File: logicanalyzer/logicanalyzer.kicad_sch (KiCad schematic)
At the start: 104 parts, among them J1 Conn_02x17_Odd_Even, J2 Conn_01x30_Pin, U1 74HC04, U2 74HC595, U3 74HC595, U4 74HC86, U5 74HC251, U6 74HC32, U7 74HC86, U8 74HC251, U9 74HC251

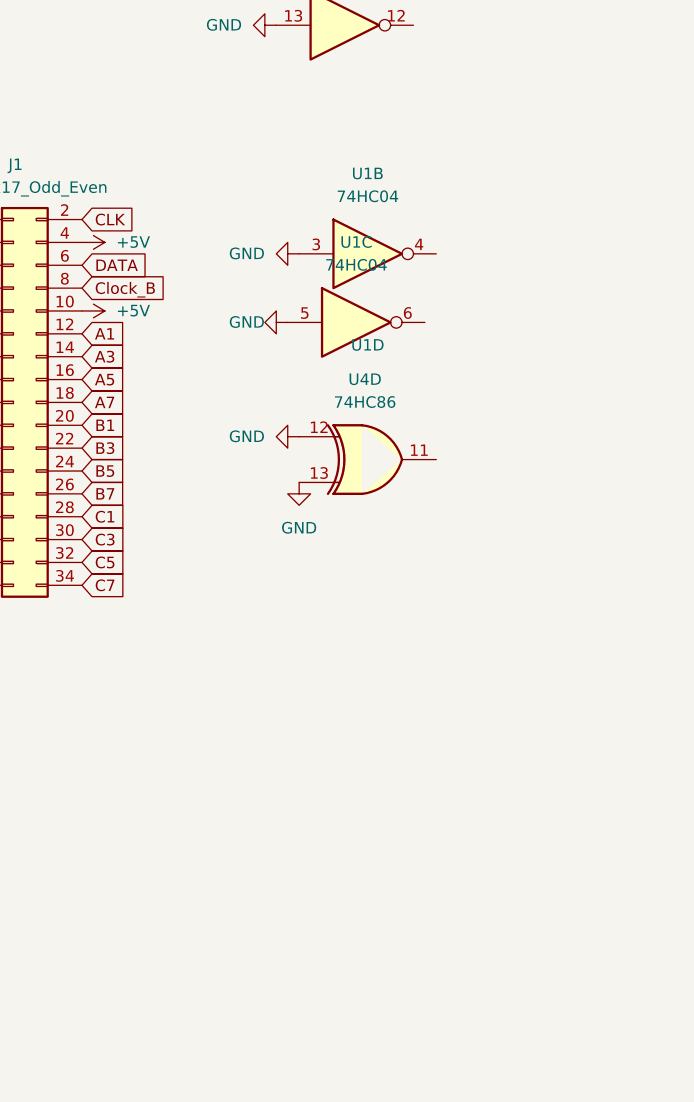
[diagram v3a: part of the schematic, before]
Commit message: Finalized PCB, added gerbers and pdf schematic
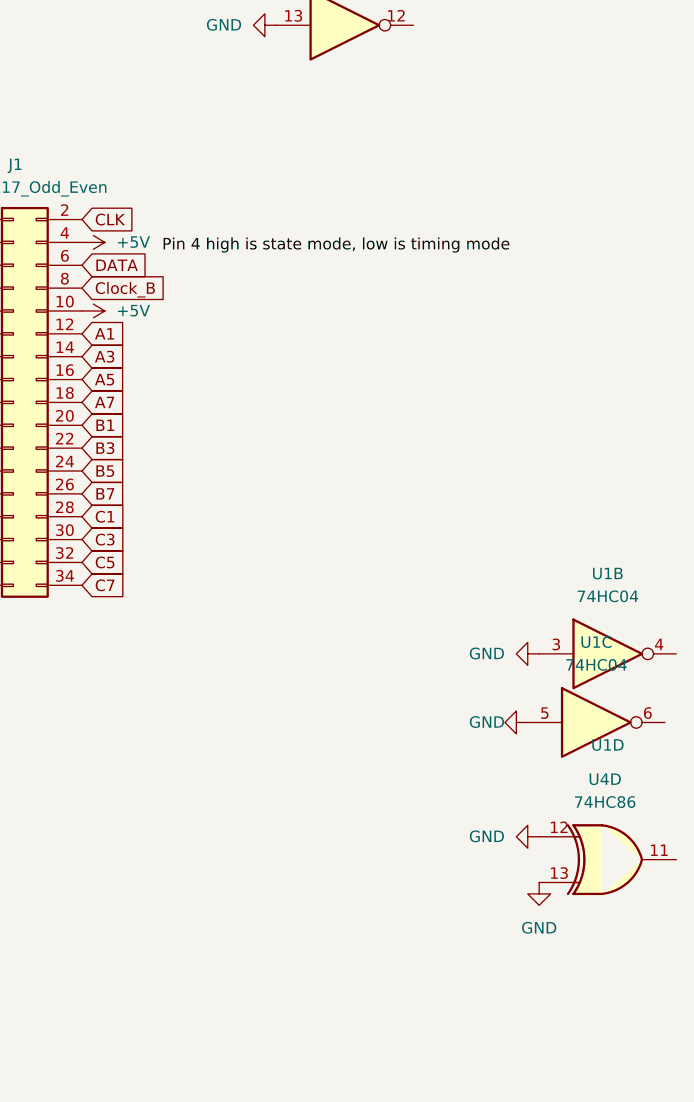
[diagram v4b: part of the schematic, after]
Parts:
- J1: footprint Connector_IDC:IDC-Header_2x17_P2.54mm_Horizontal -> Connector_IDC:IDC-Header_2x17_P2.54mm_Vertical
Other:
- moved on the sheet: U1B, U1C, U4D
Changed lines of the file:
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@@
 		)
 	)
+	(label "Pin 4 high is state mode, low is timing mode"
+		(at 344.17 134.62 0)
+		(fields_autoplaced yes)
+		(effects
+			(font
+				(size 1.27 1.27)
+			)
+			(justify left bottom)
+		)
+	)
 	(global_label "C4"
 		(shape input)
@@
 	(symbol
 		(lib_id "74xx:74HC04")
-		(at 365.76 142.24 0)
+		(at 392.43 186.69 0)
 		(unit 3)
 		(exclude_from_sim no)
@@
 		(fields_autoplaced yes)
 		(property "Reference" "U1"
-			(at 365.76 133.35 0)
+			(at 392.43 177.8 0)
 			(effects
 				(font
@@
 		)
 		(property "Value" "74HC04"
-			(at 365.76 135.89 0)
+			(at 392.43 180.34 0)
 			(effects
 				(font
@@
 		)
 		(property "Footprint" "Package_SO:SOIC-14_3.9x8.7mm_P1.27mm"
-			(at 365.76 142.24 0)
+			(at 392.43 186.69 0)
 			(effects
 				(font
@@
 		)
 		(property "Datasheet" "https://assets.nexperia.com/documents/data-sheet/74HC_HCT04.pdf"
-			(at 365.76 142.24 0)
+			(at 392.43 186.69 0)
 			(effects
 				(font
@@
 		)
 		(property "Description" "Hex Inverter"
-			(at 365.76 142.24 0)
+			(at 392.43 186.69 0)
 			(effects
 				(font
@@
 	(symbol
 		(lib_id "power:GND")
-		(at 359.41 134.62 270)
+		(at 386.08 179.07 270)
 		(unit 1)
 		(exclude_from_sim no)
@@
 		(fields_autoplaced yes)
 		(property "Reference" "#PWR021"
-			(at 353.06 134.62 0)
+			(at 379.73 179.07 0)
 			(effects
 				(font
@@
 		)
 		(property "Value" "GND"
-			(at 355.6 134.6199 90)
+			(at 382.27 179.0699 90)
 			(effects
 				(font
@@
 		)
 		(property "Footprint" ""
-			(at 359.41 134.62 0)
+			(at 386.08 179.07 0)
 			(effects
 				(font
@@
 		)
 		(property "Datasheet" ""
-			(at 359.41 134.62 0)
+			(at 386.08 179.07 0)
 			(effects
 				(font
@@
 		)
 		(property "Description" "Power symbol creates a global label with name \"GND\" , ground"
-			(at 359.41 134.62 0)
+			(at 386.08 179.07 0)
 			(effects
 				(font
@@
 			)
 		)
-		(property "Footprint" "Connector_IDC:IDC-Header_2x17_P2.54mm_Horizontal"
+		(property "Footprint" "Connector_IDC:IDC-Header_2x17_P2.54mm_Vertical"
 			(at 327.66 151.13 0)
 			(effects
@@
 	(symbol
 		(lib_id "power:GND")
-		(at 359.41 160.02 0)
+		(at 386.08 204.47 0)
 		(unit 1)
 		(exclude_from_sim no)
@@
 		(fields_autoplaced yes)
 		(property "Reference" "#PWR027"
-			(at 359.41 166.37 0)
+			(at 386.08 210.82 0)
 			(effects
 				(font
@@
 		)
 		(property "Value" "GND"
-			(at 359.41 165.1 0)
+			(at 386.08 209.55 0)
 			(effects
 				(font
@@
 		)
 		(property "Footprint" ""
-			(at 359.41 160.02 0)
+			(at 386.08 204.47 0)
 			(effects
 				(font
@@
 		)
 		(property "Datasheet" ""
-			(at 359.41 160.02 0)
+			(at 386.08 204.47 0)
 			(effects
 				(font
@@
 		)
 		(property "Description" "Power symbol creates a global label with name \"GND\" , ground"
-			(at 359.41 160.02 0)
+			(at 386.08 204.47 0)
 			(effects
 				(font
@@
 	(symbol
 		(lib_id "74xx:74HC04")
-		(at 367.03 134.62 0)
+		(at 393.7 179.07 0)
 		(unit 2)
 		(exclude_from_sim no)
@@
 		(fields_autoplaced yes)
 		(property "Reference" "U1"
-			(at 367.03 125.73 0)
+			(at 393.7 170.18 0)
 			(effects
 				(font
@@
 		)
 		(property "Value" "74HC04"
-			(at 367.03 128.27 0)
+			(at 393.7 172.72 0)
 			(effects
 				(font
@@
 		)
 		(property "Footprint" "Package_SO:SOIC-14_3.9x8.7mm_P1.27mm"
-			(at 367.03 134.62 0)
+			(at 393.7 179.07 0)
 			(effects
 				(font
@@
 		)
 		(property "Datasheet" "https://assets.nexperia.com/documents/data-sheet/74HC_HCT04.pdf"
-			(at 367.03 134.62 0)
+			(at 393.7 179.07 0)
 			(effects
 				(font
@@
 		)
 		(property "Description" "Hex Inverter"
-			(at 367.03 134.62 0)
+			(at 393.7 179.07 0)
 			(effects
 				(font
@@
 	(symbol
 		(lib_id "74xx:74HC86")
-		(at 367.03 157.48 0)
+		(at 393.7 201.93 0)
 		(unit 4)
 		(exclude_from_sim no)
@@
 		(fields_autoplaced yes)
 		(property "Reference" "U4"
-			(at 366.7252 148.59 0)
+			(at 393.3952 193.04 0)
 			(effects
 				(font
@@
 		)
 		(property "Value" "74HC86"
-			(at 366.7252 151.13 0)
+			(at 393.3952 195.58 0)
 			(effects
 				(font
@@
 		)
 		(property "Footprint" "Package_SO:SOIC-14_3.9x8.7mm_P1.27mm"
-			(at 367.03 157.48 0)
+			(at 393.7 201.93 0)
 			(effects
 				(font
@@
 		)
 		(property "Datasheet" "http://www.ti.com/lit/gpn/sn74HC86"
-			(at 367.03 157.48 0)
+			(at 393.7 201.93 0)
 			(effects
 				(font
@@
 		)
 		(property "Description" "Quad 2-input XOR"
-			(at 367.03 157.48 0)
+			(at 393.7 201.93 0)
 			(effects
 				(font
@@
 	(symbol
 		(lib_id "power:GND")
-		(at 358.14 142.24 270)
+		(at 384.81 186.69 270)
 		(unit 1)
 		(exclude_from_sim no)
@@
 		(dnp no)
 		(property "Reference" "#PWR022"
-			(at 351.79 142.24 0)
+			(at 378.46 186.69 0)
 			(effects
 				(font
@@
 		)
 		(property "Value" "GND"
-			(at 355.6 142.2399 90)
+			(at 382.27 186.6899 90)
 			(effects
 				(font
@@
 		)
 		(property "Footprint" ""
-			(at 358.14 142.24 0)
+			(at 384.81 186.69 0)
 			(effects
 				(font
@@
 		)
 		(property "Datasheet" ""
-			(at 358.14 142.24 0)
+			(at 384.81 186.69 0)
 			(effects
 				(font
@@
 		)
 		(property "Description" "Power symbol creates a global label with name \"GND\" , ground"
-			(at 358.14 142.24 0)
+			(at 384.81 186.69 0)
 			(effects
 				(font
@@
 		(dnp no)
 		(property "Reference" "U1"
-			(at 367.03 144.78 0)
+			(at 393.7 189.23 0)
 			(effects
 				(font
@@
 	(symbol
 		(lib_id "power:GND")
-		(at 359.41 154.94 270)
+		(at 386.08 199.39 270)
 		(unit 1)
 		(exclude_from_sim no)
@@
 		(fields_autoplaced yes)
 		(property "Reference" "#PWR026"
-			(at 353.06 154.94 0)
+			(at 379.73 199.39 0)
 			(effects
 				(font
@@
 		)
 		(property "Value" "GND"
-			(at 355.6 154.9399 90)
+			(at 382.27 199.3899 90)
 			(effects
 				(font
@@
 		)
 		(property "Footprint" ""
-			(at 359.41 154.94 0)
+			(at 386.08 199.39 0)
 			(effects
 				(font
@@
 		)
 		(property "Datasheet" ""
-			(at 359.41 154.94 0)
+			(at 386.08 199.39 0)
 			(effects
 				(font
@@
 		)
 		(property "Description" "Power symbol creates a global label with name \"GND\" , ground"
-			(at 359.41 154.94 0)
+			(at 386.08 199.39 0)
 			(effects
 				(font
